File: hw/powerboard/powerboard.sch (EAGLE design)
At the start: 42 parts, among them J1 ISP, J2 I2C

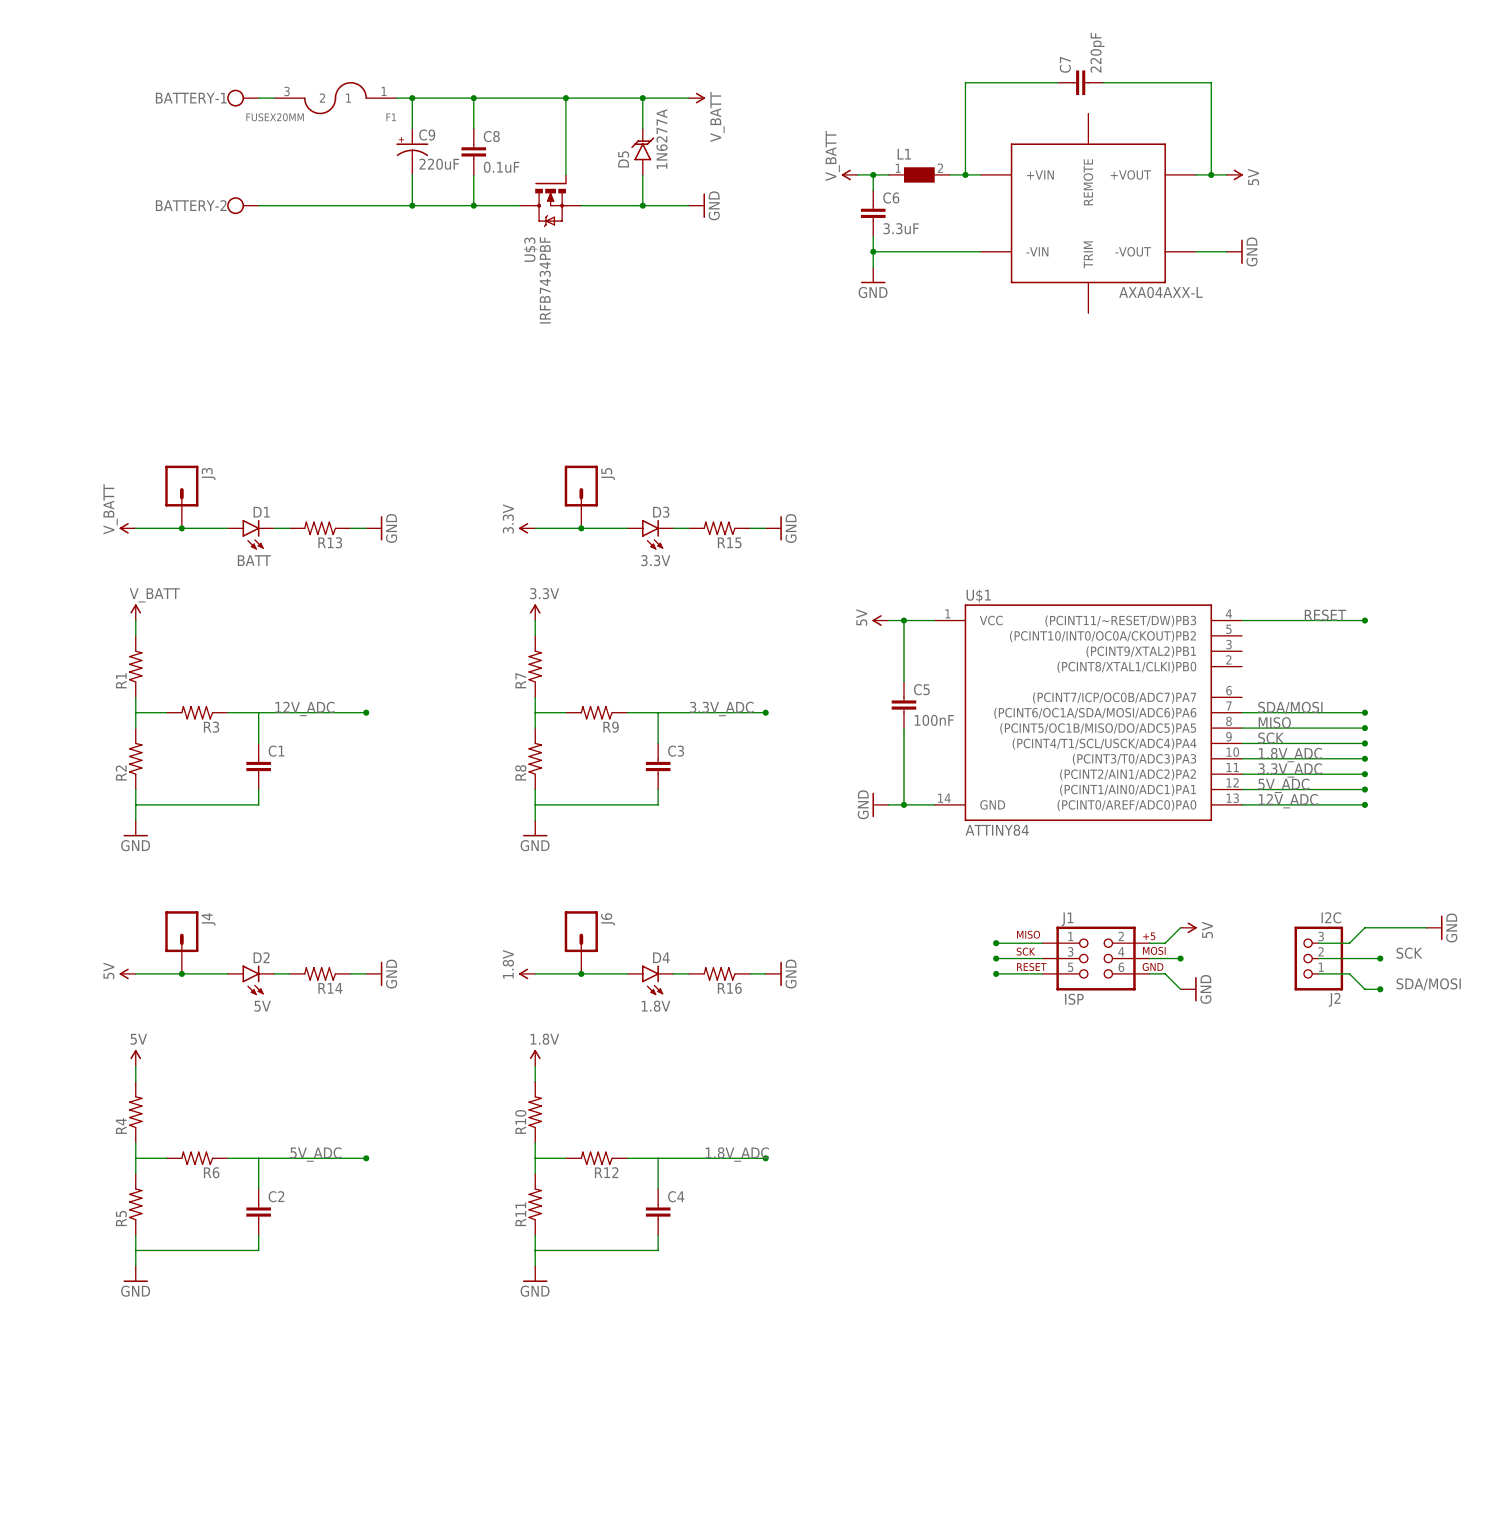
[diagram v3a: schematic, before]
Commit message: Initial commit of PowerSensor board. Decided to separate PowerBoard and PowerSensor.
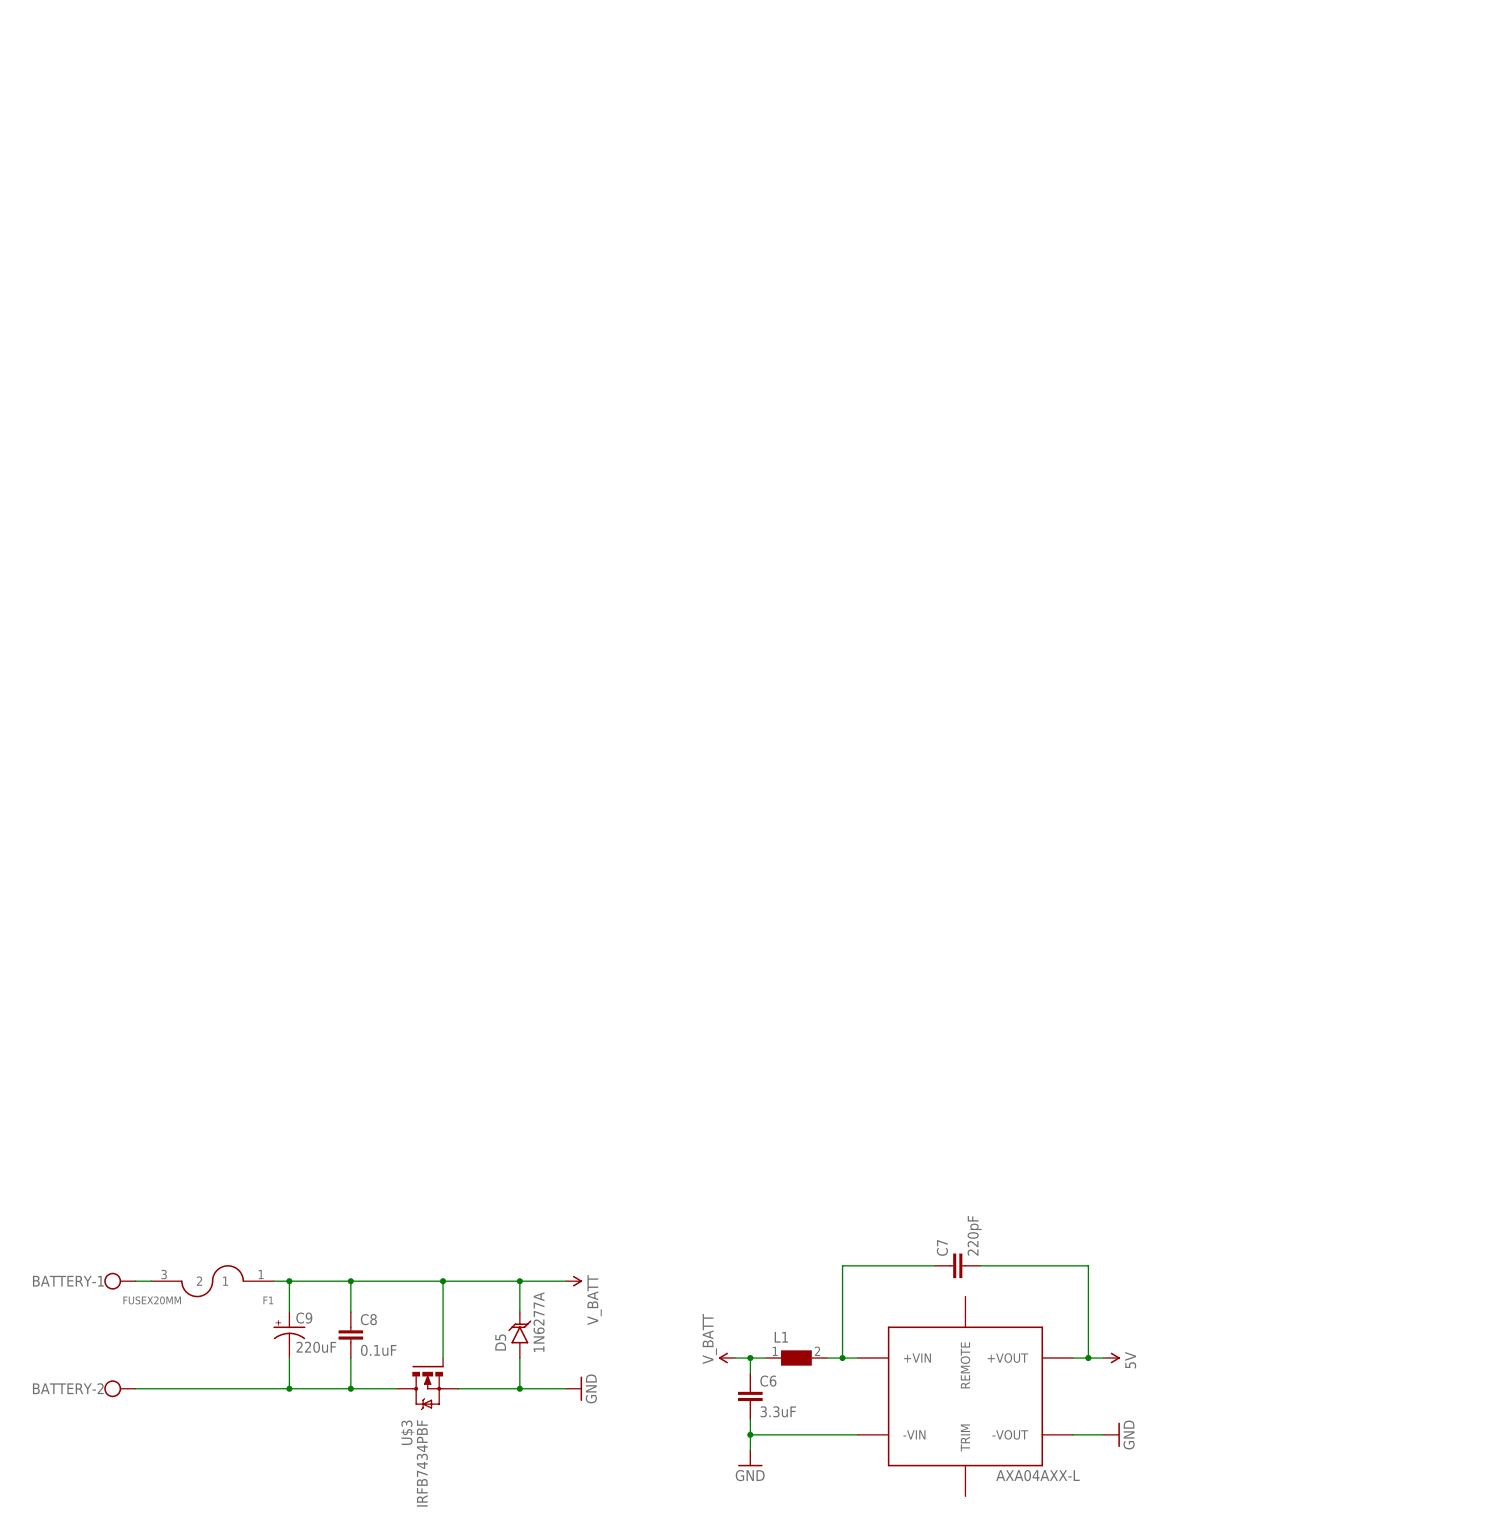
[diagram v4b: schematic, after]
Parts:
- removed C1, C2, C3, C4: (no value), SparkFun-Capacitors:CAP0603-CAP
- removed C5: 100nF, SparkFun-Capacitors:CAP0603-CAP
- removed D1: BATT, SparkFun-LED:LED0603
- removed D2: 5V, SparkFun-LED:LED0603
- removed D3: 3.3V, SparkFun-LED:LED0603
- removed D4: 1.8V, SparkFun-LED:LED0603
- removed J1: ISP, SparkFun-Connectors:AVR_SPI_PRG_6PTH
- removed J2: I2C, pinhead:PINHD-1X3/90
- removed J3, J4, J5, J6: (no value), SparkFun-Connectors:M01NOSILK-KIT
- removed R1, R10, R11, R12, R13, R14, R15, R16, R2, R3, R4, R5, R6, R7, R8, R9: (no value), SparkFun-Passives:RESISTOR0603-RES
- removed U$1: ATTINY84, SparkFun-DigitalIC:ATTINY84
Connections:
- removed net 1.8V: D4.A, J6.1, R10.2
- removed net 1.8V_ADC: C4.1, R12.1, U$1.(PCINT3/T0/ADC3)PA3
- removed net 12V_ADC: C1.1, R3.1, U$1.(PCINT0/AREF/ADC0)PA0
- removed net 3.3V: D3.A, J5.1, R7.2
- removed net 3.3V_ADC: C3.1, R9.1, U$1.(PCINT2/AIN1/ADC2)PA2
- removed net 5V_ADC: C2.1, R6.1, U$1.(PCINT1/AIN0/ADC1)PA1
- removed net MISO: J1.1, U$1.(PCINT5/OC1B/MISO/DO/ADC5)PA5
- removed net N$1: R1.1, R2.2, R3.2
- removed net N$2: R4.1, R5.2, R6.2
- removed net N$3: R7.1, R8.2, R9.2
- removed net N$4: R10.1, R11.2, R12.2
- removed net N$5: D1.C, R13.2
- removed net N$6: D2.C, R14.2
- removed net N$7: D3.C, R15.2
- removed net N$8: D4.C, R16.2
- removed net RESET: J1.5, U$1.(PCINT11/~RESET/DW)PB3
- removed net SCK: J1.3, J2.2, U$1.(PCINT4/T1/SCL/USCK/ADC4)PA4
- removed net SDA/MOSI: J1.4, J2.1, U$1.(PCINT6/OC1A/SDA/MOSI/ADC6)PA6
- net 5V: no longer C5.1, D2.A, J1.2, J4.1, R4.2, U$1.VCC
- net GND: no longer C1.2, C2.2, C3.2, C4.2, C5.2, J1.6, J2.3, R11.1, R13.1, R14.1, R15.1, R16.1, R2.1, R5.1, R8.1, U$1.GND
- net V_BATT: no longer D1.A, J3.1, R1.2
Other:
- moved on the sheet: BATTERY-1, BATTERY-2, C6, C7, C8, C9, D5, F1, L1, U$3
